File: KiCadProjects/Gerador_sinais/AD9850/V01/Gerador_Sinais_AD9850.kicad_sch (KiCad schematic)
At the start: 22 parts, among them J1 alimentacao analogica, J2 sinais analogicos, J3 comunicacao / sinais digitais, J4 3.3V STM32, J5 5.0V STM32, U1 AD9850_module, U2 BluePill_STM32F103C, U3 AD828AN, U4 X9c10x, U5 X9c10x

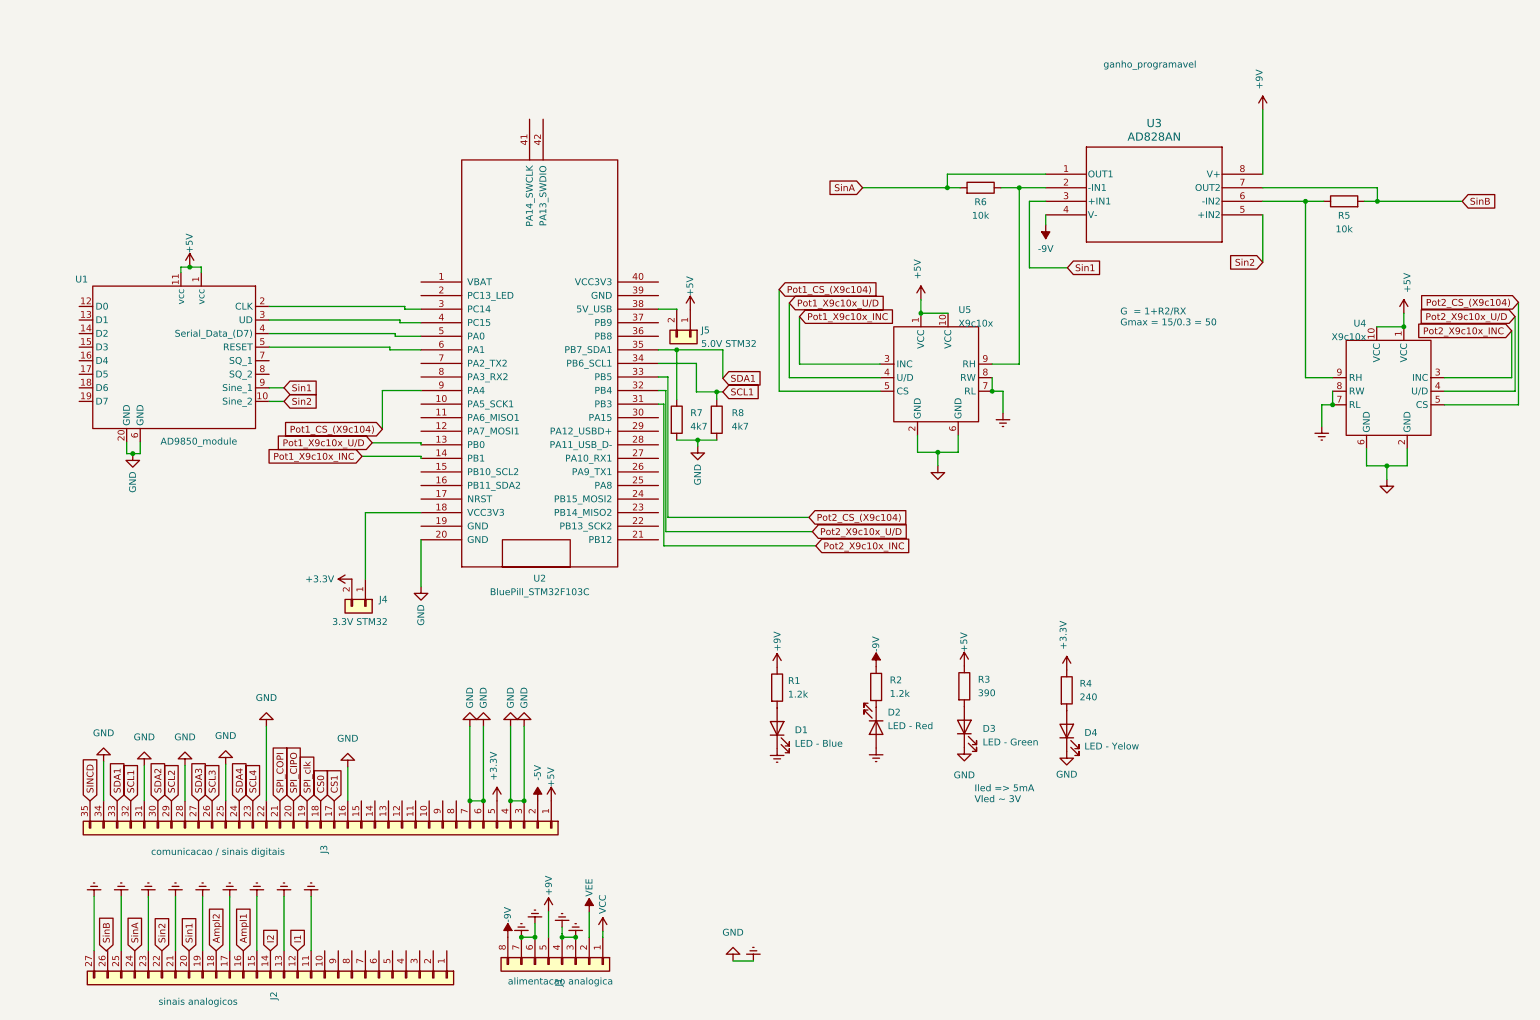
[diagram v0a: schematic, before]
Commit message: mudanca sinais de entrada e largura trilha
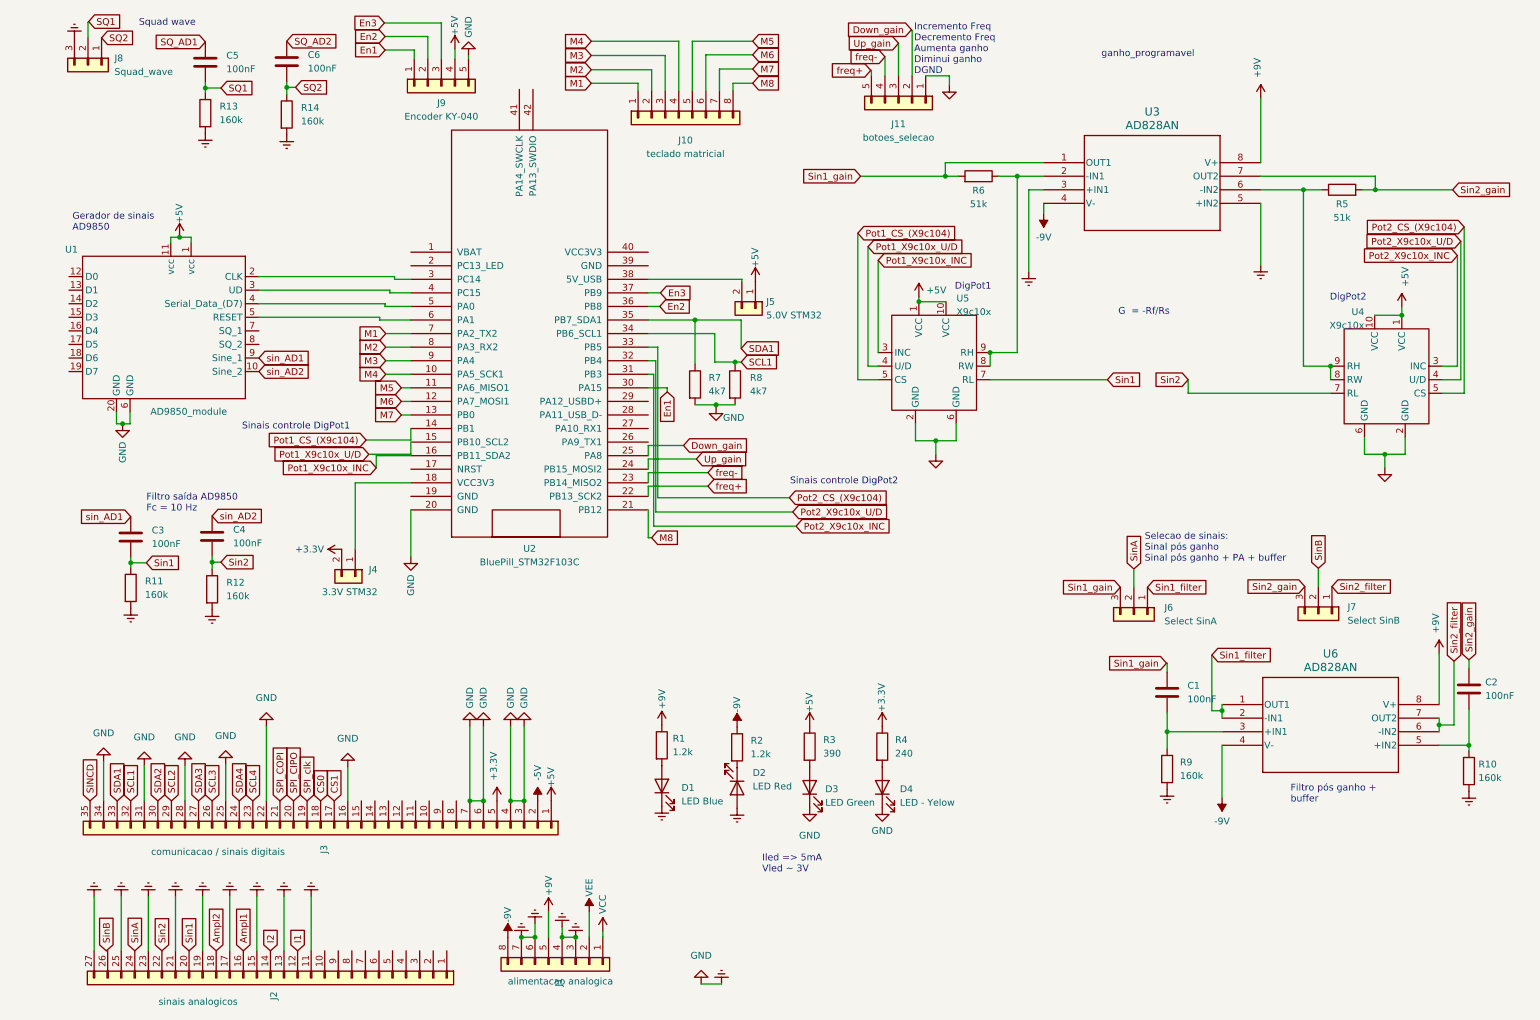
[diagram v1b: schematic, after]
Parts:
- added C1, C2, C3, C4, C5, C6: 100nF, Capacitor_THT:C_Disc_D3.0mm_W1.6mm_P2.50mm, symbol Device:C
- added J10: teclado matricial, Connector_PinHeader_2.54mm:PinHeader_1x08_P2.54mm_Horizontal, symbol Connector_Generic:Conn_01x08
- added J11: botoes_selecao, Connector_PinHeader_2.54mm:PinHeader_1x05_P2.54mm_Horizontal, symbol Connector_Generic:Conn_01x05
- added J6: Select SinA, Connector_PinHeader_2.54mm:PinHeader_1x03_P2.54mm_Vertical, symbol Connector_Generic:Conn_01x03
- added J7: Select SinB, Connector_PinHeader_2.54mm:PinHeader_1x03_P2.54mm_Vertical, symbol Connector_Generic:Conn_01x03
- added J8: Squad_wave, Connector_PinHeader_2.54mm:PinHeader_1x03_P2.54mm_Vertical, symbol Connector_Generic:Conn_01x03
- added J9: Encoder KY-040, Connector_PinHeader_2.54mm:PinHeader_1x05_P2.54mm_Vertical, symbol Connector_Generic:Conn_01x05
- added R10, R11, R12, R13, R14, R9: 160k, Resistor_THT:R_Axial_DIN0207_L6.3mm_D2.5mm_P7.62mm_Horizontal, symbol Device:R
- added U6: AD828AN, AD828:AD828, symbol AD828AN:AD828AN
- D1: value LED - Blue -> LED Blue
- D2: value LED - Red -> LED Red
- D3: value LED - Green -> LED Green
- J4, J5: footprint (none) -> Connector_PinHeader_2.54mm:PinHeader_1x02_P2.54mm_Vertical
- R5, R6: value 10k -> 51k
- R7, R8: footprint (none) -> Resistor_THT:R_Axial_DIN0207_L6.3mm_D2.5mm_P7.62mm_Horizontal
- U2: footprint BluePill_breakouts:BluePill_STM32F103C -> BluePill_STM32:BluePill_STM32F103C
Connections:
- net +5V: now also J9.4 (Pin_4)
- net +9V: now also U6.8 (V+)
- net -9V: now also U6.4 (V-)
- net Earth: now also U3.3 (+IN1), U3.5 (+IN2), J11.1 (Pin_1), J8.3 (Pin_3), J9.5 (Pin_5), R10.2, R11.2, R12.2, R13.2, R14.2, R9.2; no longer U4.7 (RL), U4.8 (RW), U5.7 (RL), U5.8 (RW)
- net Pot1_CS_(X9c104): now also U2.14 (PB1); no longer U2.9 (PA4)
- net Pot1_X9c10x_INC: now also U2.16 (PB11_SDA2); no longer U2.14 (PB1)
- net Pot1_X9c10x_U/D: now also U2.15 (PB10_SCL2); no longer U2.13 (PB0)
- net Sin1: now also U5.7 (RL), C3.2, R11.1; no longer U1.9 (Sine_1), U3.3 (+IN1)
- net Sin2: now also U4.7 (RL), C4.2, R12.1; no longer U1.10 (Sine_2), U3.5 (+IN2)
- net SinA: now also J6.2 (Pin_2); no longer R6.2, U3.1 (OUT1)
- net SinB: now also J7.2 (Pin_2); no longer R5.2, U3.7 (OUT2)
- net at R6.1, U3.2 (-IN1), U5.9 (RH): now also U5.8 (RW)
- net M4: now reaches U2.10 (PA5_SCK1)
- net M4: now also J10.4 (Pin_4)
- net M5: now reaches U2.11 (PA6_MISO1)
- net M5: now also J10.5 (Pin_5)
- net M6: now reaches U2.12 (PA7_MOSI1)
- net M6: now also J10.6 (Pin_6)
- net M8: now reaches U2.21 (PB12)
- net M8: now also J10.8 (Pin_8)
- net freq+: now reaches U2.22 (PB13_SCK2)
- net freq+: now also J11.5 (Pin_5)
- net freq-: now reaches U2.23 (PB14_MISO2)
- net freq-: now also J11.4 (Pin_4)
- net Up_gain: now reaches U2.24 (PB15_MOSI2)
- net Up_gain: now also J11.3 (Pin_3)
- net Down_gain: now reaches U2.25 (PA8)
- net Down_gain: now also J11.2 (Pin_2)
- net En1: now reaches U2.30 (PA15)
- net En1: now also J9.1 (Pin_1)
- net En2: now reaches U2.36 (PB8)
- net En2: now also J9.2 (Pin_2)
- net En3: now reaches U2.37 (PB9)
- net En3: now also J9.3 (Pin_3)
- net M1: now reaches U2.7 (PA2_TX2)
- net M1: now also J10.1 (Pin_1)
- net M2: now reaches U2.8 (PA3_RX2)
- net M2: now also J10.2 (Pin_2)
- net at R5.1, U3.6 (-IN2), U4.9 (RH): now also U4.8 (RW)
- new net: C1.2, R9.1, U6.3 (+IN1)
- new net: C2.2, R10.1, U6.5 (+IN2)
- new net M3: J10.3 (Pin_3), U2.9 (PA4)
- new net M7: J10.7 (Pin_7), U2.13 (PB0)
- new net SQ1: C5.2, J8.2 (Pin_2), R13.1
- new net SQ2: C6.2, J8.1 (Pin_1), R14.1
- new net SQ_AD1: C5.1
- new net SQ_AD2: C6.1
- new net Sin1_filter: J6.1 (Pin_1), U6.1 (OUT1), U6.2 (-IN1)
- new net Sin1_gain: C1.1, J6.3 (Pin_3), R6.2, U3.1 (OUT1)
- new net Sin2_filter: J7.1 (Pin_1), U6.6 (-IN2), U6.7 (OUT2)
- new net Sin2_gain: C2.1, J7.3 (Pin_3), R5.2, U3.7 (OUT2)
- new net sin_AD1: C3.1, U1.9 (Sine_1)
- new net sin_AD2: C4.1, U1.10 (Sine_2)
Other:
- note added: "DigPot1"
- note added: "DigPot2"
- note added: "Filtro pós ganho + buffer"
- note added: "Filtro saída AD9850 Fc = 10 Hz"
- note added: "G = -Rf/Rs"
- note added: "Gerador de sinais AD9850"
- note added: "Incremento Freq Decremento Freq Aumenta ganho Diminui ganho DGND"
- note added: "Selecao de sinais: Sinal pós ganho Sinal pós ganho + PA + buffer"
- note added: "Sinais controle DigPot1"
- note added: "Sinais controle DigPot2"
- note added: "Squad wave"
- note removed: "G = 1+R2/RX Gmax = 15/0.3 = 50"
- moved on the sheet: D1, D2, D3, D4, J4, J5, R1, R2, R3, R4, R5, R6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

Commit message: todas conexoes feitas
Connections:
- net +3.3V: now also R7.2, R8.2
- net Ampl1: now also U2.9 (PA4)
- net Ampl2: now also U2.10 (PA5_SCK1)
- net Earth: no longer R7.2, R8.2
- net M3: now also U2.29 (PA12_USBD+); no longer U2.9 (PA4)
- net M4: now also U2.28 (PA11_USB_D-); no longer U2.10 (PA5_SCK1)
- net SQ_AD1: now also U1.7 (SQ_1)
- net SQ_AD2: now also U1.8 (SQ_2)
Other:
- moved on the sheet: J5, R7, R8

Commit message: Baseado barramento v04 - Finalizado
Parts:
- renumbered D4 to L+3.3v1, D3 to L+5v1, D1 to L+9v1, D2 to L-9v1, U1 to U1-AD9850, U3 to U3-ganho1, U4 to U4-DigPot2, U5 to U5-DigPot1, U6 to U6-filtro-saida1
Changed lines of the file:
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@@
   (symbol (lib_id "Device:LED") (at 151.765 157.226 90) (unit 1)
     (in_bom yes) (on_board yes) (dnp no) (fields_autoplaced)
-    (property "Reference" "D3" (at 154.686 157.5435 90)
+    (property "Reference" "L+5v1" (at 154.94 157.5435 90)
       (effects (font (size 1.27 1.27)) (justify right))
     )
-    (property "Value" "LED Green" (at 154.686 160.0835 90)
+    (property "Value" "LED Green" (at 154.94 160.0835 90)
       (effects (font (size 1.27 1.27)) (justify right))
     )
@@
       (project "Gerador_Sinais_AD9850"
         (path "/f0ff92cf-26e5-4ab9-977d-5f9689e8a5d0"
-          (reference "D3") (unit 1)
+          (reference "L+5v1") (unit 1)
         )
       )
@@
   (symbol (lib_id "Device:LED") (at 124.079 156.972 90) (unit 1)
     (in_bom yes) (on_board yes) (dnp no) (fields_autoplaced)
-    (property "Reference" "D1" (at 127.762 157.2895 90)
+    (property "Reference" "L+9v1" (at 127 157.2895 90)
       (effects (font (size 1.27 1.27)) (justify right))
     )
-    (property "Value" "LED Blue" (at 127.762 159.8295 90)
+    (property "Value" "LED Blue" (at 127 159.8295 90)
       (effects (font (size 1.27 1.27)) (justify right))
     )
@@
       (project "Gerador_Sinais_AD9850"
         (path "/f0ff92cf-26e5-4ab9-977d-5f9689e8a5d0"
-          (reference "D1") (unit 1)
+          (reference "L+9v1") (unit 1)
         )
       )
@@
   )
   (symbol (lib_id "X9c10X_module:X9c10X_module") (at 174.752 78.359 0) (unit 1)
-    (in_bom yes) (on_board yes) (dnp no) (fields_autoplaced)
-    (property "Reference" "U5" (at 179.2479 65.659 0)
-      (effects (font (size 1.27 1.27)) (justify left))
-    )
-    (property "Value" "X9c10x" (at 179.2479 68.199 0)
+    (in_bom yes) (on_board yes) (dnp no)
+    (property "Reference" "U5-DigPot1" (at 182.372 90.932 0)
+      (effects (font (size 1.27 1.27)) (justify left))
+    )
+    (property "Value" "X9c10x" (at 179.4861 66.04 0)
       (effects (font (size 1.27 1.27)) (justify left))
     )
@@
       (project "Gerador_Sinais_AD9850"
         (path "/f0ff92cf-26e5-4ab9-977d-5f9689e8a5d0"
-          (reference "U5") (unit 1)
+          (reference "U5-DigPot1") (unit 1)
         )
       )
@@
   (symbol (lib_id "AD828AN:AD828AN") (at 228.981 141.732 0) (unit 1)
     (in_bom yes) (on_board yes) (dnp no)
-    (property "Reference" "U6" (at 249.301 132.207 0)
+    (property "Reference" "U6-filtro-saida1" (at 249.301 132.207 0)
       (effects (font (size 1.524 1.524)))
     )
@@
       (project "Gerador_Sinais_AD9850"
         (path "/f0ff92cf-26e5-4ab9-977d-5f9689e8a5d0"
-          (reference "U6") (unit 1)
+          (reference "U6-filtro-saida1") (unit 1)
         )
       )
@@
   (symbol (lib_id "AD828AN:AD828AN") (at 195.58 40.259 0) (unit 1)
     (in_bom yes) (on_board yes) (dnp no)
-    (property "Reference" "U3" (at 215.9 30.734 0)
+    (property "Reference" "U3-ganho1" (at 215.9 30.734 0)
       (effects (font (size 1.524 1.524)))
     )
@@
       (project "Gerador_Sinais_AD9850"
         (path "/f0ff92cf-26e5-4ab9-977d-5f9689e8a5d0"
-          (reference "U3") (unit 1)
+          (reference "U3-ganho1") (unit 1)
         )
       )
@@
   (symbol (lib_id "Device:LED") (at 138.176 157.353 270) (unit 1)
     (in_bom yes) (on_board yes) (dnp no) (fields_autoplaced)
-    (property "Reference" "D2" (at 141.097 154.4955 90)
-      (effects (font (size 1.27 1.27)) (justify left))
-    )
-    (property "Value" "LED Red" (at 141.097 157.0355 90)
+    (property "Reference" "L-9v1" (at 140.97 154.4955 90)
+      (effects (font (size 1.27 1.27)) (justify left))
+    )
+    (property "Value" "LED Red" (at 140.97 157.0355 90)
       (effects (font (size 1.27 1.27)) (justify left))
     )
@@
       (project "Gerador_Sinais_AD9850"
         (path "/f0ff92cf-26e5-4ab9-977d-5f9689e8a5d0"
-          (reference "D2") (unit 1)
+          (reference "L-9v1") (unit 1)
         )
       )
@@
   (symbol (lib_id "AD9850_module:AD9850_module") (at 30.861 71.755 0) (mirror y) (unit 1)
     (in_bom yes) (on_board yes) (dnp no)
-    (property "Reference" "U1" (at 14.732 56.515 0)
+    (property "Reference" "U1-AD9850" (at 14.732 56.515 0)
       (effects (font (size 1.27 1.27)) (justify left))
     )
@@
       (project "Gerador_Sinais_AD9850"
         (path "/f0ff92cf-26e5-4ab9-977d-5f9689e8a5d0"
-          (reference "U1") (unit 1)
+          (reference "U1-AD9850") (unit 1)
         )
       )
@@
   (symbol (lib_id "Device:LED") (at 165.354 157.226 90) (unit 1)
     (in_bom yes) (on_board yes) (dnp no) (fields_autoplaced)
-    (property "Reference" "D4" (at 168.656 157.5435 90)
+    (property "Reference" "L+3.3v1" (at 168.91 157.5435 90)
       (effects (font (size 1.27 1.27)) (justify right))
     )
-    (property "Value" "LED - Yelow" (at 168.656 160.0835 90)
+    (property "Value" "LED - Yelow" (at 168.91 160.0835 90)
       (effects (font (size 1.27 1.27)) (justify right))
     )
@@
       (project "Gerador_Sinais_AD9850"
         (path "/f0ff92cf-26e5-4ab9-977d-5f9689e8a5d0"
-          (reference "D4") (unit 1)
+          (reference "L+3.3v1") (unit 1)
         )
       )
@@
   (symbol (lib_id "X9c10X_module:X9c10X_module") (at 260.096 80.899 0) (mirror y) (unit 1)
     (in_bom yes) (on_board yes) (dnp no) (fields_autoplaced)
-    (property "Reference" "U4" (at 255.6001 68.199 0)
-      (effects (font (size 1.27 1.27)) (justify left))
-    )
-    (property "Value" "X9c10x" (at 255.6001 70.739 0)
-      (effects (font (size 1.27 1.27)) (justify left))
+    (property "Reference" "U4-DigPot2" (at 266.2621 66.04 0)
+      (effects (font (size 1.27 1.27)) (justify right))
+    )
+    (property "Value" "X9c10x" (at 266.2621 68.58 0)
+      (effects (font (size 1.27 1.27)) (justify right))
     )
     (property "Footprint" "X9c10X_module:X9c10X_module" (at 258.826 80.899 0)
@@
       (project "Gerador_Sinais_AD9850"
         (path "/f0ff92cf-26e5-4ab9-977d-5f9689e8a5d0"
-          (reference "U4") (unit 1)
-        )
-      )
+          (reference "U4-DigPot2") (unit 1)
+        )
+      )

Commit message: temp
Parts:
- added U7-bufferAD9850: AD828AN, AD828:AD828, symbol AD828:AD828AN
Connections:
- net +9V: now also U7-bufferAD9850.8 (V+)
- net -9V: now also U7-bufferAD9850.4 (V-)
- net Sin1: now also U7-bufferAD9850.1 (OUT1), U7-bufferAD9850.2 (-IN1); no longer C3.2, R11.1
- net Sin2: now also U7-bufferAD9850.6 (-IN2), U7-bufferAD9850.7 (OUT2); no longer C4.2, R12.1
- new net Sin1_PA: C3.2, R11.1, U7-bufferAD9850.3 (+IN1)
- new net Sin2_PA: C4.2, R12.1, U7-bufferAD9850.5 (+IN2)
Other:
- moved on the sheet: C3, C4, J1, J2, J3, L+3.3v1, L+5v1, L+9v1, L-9v1, R1, R11, R12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

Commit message: temp
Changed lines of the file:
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@@
     (stroke (width 0) (type default))
   )
-  (wire (pts (xy 181.991 151.257) (xy 185.801 151.257))
+  (wire (pts (xy 188.087 160.909) (xy 191.897 160.909))
     (stroke (width 0) (type default))
   )
@@
     )
   )
-  (symbol (lib_id "power:GND") (at 181.991 151.257 180) (unit 1)
+  (symbol (lib_id "power:GND") (at 188.087 160.909 180) (unit 1)
     (in_bom yes) (on_board yes) (dnp no) (fields_autoplaced)
-    (property "Reference" "#PWR017" (at 181.991 144.907 0)
+    (property "Reference" "#PWR017" (at 188.087 154.559 0)
       (effects (font (size 1.27 1.27)) hide)
     )
-    (property "Value" "GND" (at 181.991 145.923 0)
+    (property "Value" "GND" (at 188.087 155.575 0)
       (effects (font (size 1.27 1.27)))
     )
-    (property "Footprint" "" (at 181.991 151.257 0)
+    (property "Footprint" "" (at 188.087 160.909 0)
       (effects (font (size 1.27 1.27)) hide)
     )
-    (property "Datasheet" "" (at 181.991 151.257 0)
+    (property "Datasheet" "" (at 188.087 160.909 0)
       (effects (font (size 1.27 1.27)) hide)
     )
@@
     )
   )
-  (symbol (lib_id "power:Earth") (at 185.801 151.257 180) (unit 1)
+  (symbol (lib_id "power:Earth") (at 191.897 160.909 180) (unit 1)
     (in_bom yes) (on_board yes) (dnp no) (fields_autoplaced)
-    (property "Reference" "#PWR052" (at 185.801 144.907 0)
+    (property "Reference" "#PWR052" (at 191.897 154.559 0)
       (effects (font (size 1.27 1.27)) hide)
     )
-    (property "Value" "Earth" (at 185.801 147.447 0)
+    (property "Value" "Earth" (at 191.897 157.099 0)
       (effects (font (size 1.27 1.27)) hide)
     )
-    (property "Footprint" "" (at 185.801 151.257 0)
+    (property "Footprint" "" (at 191.897 160.909 0)
       (effects (font (size 1.27 1.27)) hide)
     )
-    (property "Datasheet" "~" (at 185.801 151.257 0)
+    (property "Datasheet" "~" (at 191.897 160.909 0)
       (effects (font (size 1.27 1.27)) hide)
     )

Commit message: V01aCopia: menor, com vias. V01a: maior, sem vias
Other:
- title: Barramento V04 -> Gerador de sinais AD9850
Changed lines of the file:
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@@
   (paper "A4")
   (title_block
-    (title "Barramento V04")
+    (title "Gerador de sinais AD9850")
     (date "2024-02-05")
-    (rev "v04")
+    (rev "v02")
     (company "EITduino")
     (comment 1 "Autor: Gustavo Pinheiro")
-    (comment 2 "Barramento proposto para uma placa 90x100 mm")
-    (comment 3 "Placa face dupla")
-    (comment 4 "Pinos AGND e DGND")
-    (comment 5 "capacitor 100nF ceramico")
-    (comment 6 "capacitores uF tantalo")
+    (comment 2 "Placa face dupla 100x100 mm")
+    (comment 3 "potenciometro digital: x9c104 (100k)")
+    (comment 4 "Baseado no barramento V05")
   )
   (junction (at 160.0188 185.42) (diameter 0) (color 0 0 0 0)
